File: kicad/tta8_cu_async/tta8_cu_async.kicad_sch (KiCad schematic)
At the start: 23 parts, among them J1 Conn_02x32_Counter_Clockwise, J2 Conn_01x06, J3 Conn_02x02_Odd_Even, U1 74AHCT74, U10 74HCT193, U11 74HCT193, U12 74AHCT00, U13 74AHCT573, U14 74AHCT573, U15 74AHCT573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

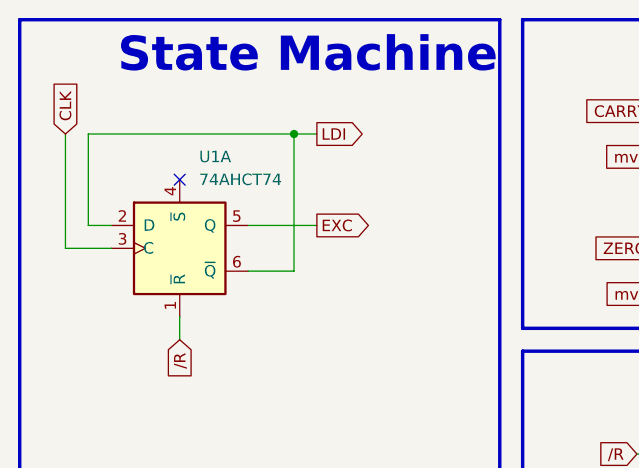
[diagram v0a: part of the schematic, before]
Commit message: Fix floating /S in State Machine
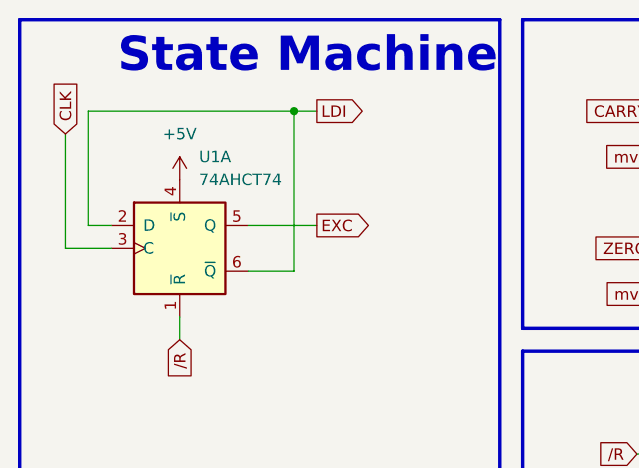
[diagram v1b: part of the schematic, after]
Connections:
- net +5V: now also U1.4 (~{S})
- no-connect marks 26 -> 25
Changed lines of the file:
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@@
 	)
 	(junction
-		(at 369.57 104.14)
+		(at 44.45 24.13)
 		(diameter 0)
 		(color 0 0 0 0)
 	)
 	(junction
-		(at 44.45 26.67)
+		(at 369.57 104.14)
 		(diameter 0)
 		(color 0 0 0 0)
@@
 	)
 	(no_connect
-		(at 31.75 31.75)
-	)
-	(no_connect
 		(at 73.66 138.43)
 	)
@@
 	(wire
 		(pts
-			(xy 44.45 26.67) (xy 46.99 26.67)
+			(xy 44.45 24.13) (xy 46.99 24.13)
 		)
 		(stroke
@@
 	(wire
 		(pts
-			(xy 44.45 26.67) (xy 21.59 26.67)
+			(xy 44.45 24.13) (xy 21.59 24.13)
 		)
 		(stroke
@@
 	(wire
 		(pts
-			(xy 44.45 26.67) (xy 44.45 41.91)
-		)
-		(stroke
-			(width 0)
-			(type default)
-		)
-	)
-	(wire
-		(pts
 			(xy 250.19 43.18) (xy 254 43.18)
 		)
@@
 	(wire
 		(pts
-			(xy 21.59 26.67) (xy 21.59 36.83)
+			(xy 21.59 24.13) (xy 21.59 36.83)
 		)
 		(stroke
@@
 	(wire
 		(pts
+			(xy 44.45 24.13) (xy 44.45 41.91)
+		)
+		(stroke
+			(width 0)
+			(type default)
+		)
+	)
+	(wire
+		(pts
 			(xy 125.73 133.35) (xy 125.73 135.89)
 		)
@@
 	(global_label "LDI"
 		(shape output)
-		(at 46.99 26.67 0)
+		(at 46.99 24.13 0)
 		(fields_autoplaced yes)
 		(effects
@@
 		)
 		(property "Intersheetrefs" "${INTERSHEET_REFS}"
-			(at 52.8781 26.67 0)
+			(at 52.8781 24.13 0)
 			(effects
 				(font
@@
 				)
 			)
+		)
+	)
+	(symbol
+		(lib_id "power:+5V")
+		(at 31.75 31.75 0)
+		(unit 1)
+		(exclude_from_sim no)
+		(in_bom yes)
+		(on_board yes)
+		(dnp no)
+		(fields_autoplaced yes)
+		(property "Reference" "#PWR03"
+			(at 31.75 35.56 0)
+			(effects
+				(font
+					(size 1.27 1.27)
+				)
+				(hide yes)
+			)
+		)
+		(property "Value" "+5V"
+			(at 31.75 26.67 0)
+			(effects
+				(font
+					(size 1.27 1.27)
+				)
+			)
+		)
+		(property "Footprint" ""
+			(at 31.75 31.75 0)
+			(effects
+				(font
+					(size 1.27 1.27)
+				)
+				(hide yes)
+			)
+		)
+		(property "Datasheet" ""
+			(at 31.75 31.75 0)
+			(effects
+				(font
+					(size 1.27 1.27)
+				)
+				(hide yes)
+			)
+		)
+		(property "Description" "Power symbol creates a global label with name \"+5V\""
+			(at 31.75 31.75 0)
+			(effects
+				(font
+					(size 1.27 1.27)
+				)
+				(hide yes)
+			)
+		)
+		(pin "1"
+		)
+		(instances
+			(project "tta8_cu_async"
+				(path "/ee320d24-5d9c-4c33-80b6-742ba44744c6"
+					(reference "#PWR03")
+					(unit 1)
+				)
+			)

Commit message: cu change to sockets
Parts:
- U1, U12, U2, U3: footprint Package_DIP:DIP-14_W7.62mm -> Package_DIP:DIP-14_W7.62mm_Socket
- U10, U11, U5, U6, U7, U8, U9: footprint Package_DIP:DIP-16_W7.62mm -> Package_DIP:DIP-16_W7.62mm_Socket
- U13, U14, U15, U16, U4: footprint Package_DIP:DIP-20_W7.62mm -> Package_DIP:DIP-20_W7.62mm_Socket
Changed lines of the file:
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@@
 			)
 		)
-		(property "Footprint" "Package_DIP:DIP-20_W7.62mm"
+		(property "Footprint" "Package_DIP:DIP-20_W7.62mm_Socket"
 			(at 237.49 53.34 0)
 			(effects
@@
 			)
 		)
-		(property "Footprint" "Package_DIP:DIP-14_W7.62mm"
+		(property "Footprint" "Package_DIP:DIP-14_W7.62mm_Socket"
 			(at 344.17 212.09 0)
 			(effects
@@
 			)
 		)
-		(property "Footprint" "Package_DIP:DIP-14_W7.62mm"
+		(property "Footprint" "Package_DIP:DIP-14_W7.62mm_Socket"
 			(at 322.58 212.09 0)
 			(effects
@@
 			)
 		)
-		(property "Footprint" "Package_DIP:DIP-20_W7.62mm"
+		(property "Footprint" "Package_DIP:DIP-20_W7.62mm_Socket"
 			(at 36.83 105.41 0)
 			(effects
@@
 			)
 		)
-		(property "Footprint" "Package_DIP:DIP-14_W7.62mm"
+		(property "Footprint" "Package_DIP:DIP-14_W7.62mm_Socket"
 			(at 115.57 34.29 0)
 			(effects
@@
 			)
 		)
-		(property "Footprint" "Package_DIP:DIP-20_W7.62mm"
+		(property "Footprint" "Package_DIP:DIP-20_W7.62mm_Socket"
 			(at 384.81 106.68 0)
 			(effects
@@
 			)
 		)
-		(property "Footprint" "Package_DIP:DIP-16_W7.62mm"
+		(property "Footprint" "Package_DIP:DIP-16_W7.62mm_Socket"
 			(at 63.5 130.81 0)
 			(effects
@@
 			)
 		)
-		(property "Footprint" "Package_DIP:DIP-14_W7.62mm"
+		(property "Footprint" "Package_DIP:DIP-14_W7.62mm_Socket"
 			(at 95.25 41.91 0)
 			(effects
@@
 			)
 		)
-		(property "Footprint" "Package_DIP:DIP-16_W7.62mm"
+		(property "Footprint" "Package_DIP:DIP-16_W7.62mm_Socket"
 			(at 280.67 106.68 0)
 			(effects
@@
 			)
 		)
-		(property "Footprint" "Package_DIP:DIP-16_W7.62mm"
+		(property "Footprint" "Package_DIP:DIP-16_W7.62mm_Socket"
 			(at 137.16 130.81 0)
 			(effects
@@
 			)
 		)
-		(property "Footprint" "Package_DIP:DIP-14_W7.62mm"
+		(property "Footprint" "Package_DIP:DIP-14_W7.62mm_Socket"
 			(at 375.92 140.97 0)
 			(effects
@@
 			)
 		)
-		(property "Footprint" "Package_DIP:DIP-14_W7.62mm"
+		(property "Footprint" "Package_DIP:DIP-14_W7.62mm_Socket"
 			(at 391.16 176.53 0)
 			(effects
@@
 			)
 		)
-		(property "Footprint" "Package_DIP:DIP-20_W7.62mm"
+		(property "Footprint" "Package_DIP:DIP-20_W7.62mm_Socket"
 			(at 318.77 53.34 0)
 			(effects
@@
 			)
 		)
-		(property "Footprint" "Package_DIP:DIP-14_W7.62mm"
+		(property "Footprint" "Package_DIP:DIP-14_W7.62mm_Socket"
 			(at 133.35 36.83 0)
 			(effects
@@
 			)
 		)
-		(property "Footprint" "Package_DIP:DIP-14_W7.62mm"
+		(property "Footprint" "Package_DIP:DIP-14_W7.62mm_Socket"
 			(at 345.44 176.53 0)
 			(effects
@@
 			)
 		)
-		(property "Footprint" "Package_DIP:DIP-14_W7.62mm"
+		(property "Footprint" "Package_DIP:DIP-14_W7.62mm_Socket"
 			(at 203.2 66.04 0)
 			(effects
@@
 			)
 		)
-		(property "Footprint" "Package_DIP:DIP-16_W7.62mm"
+		(property "Footprint" "Package_DIP:DIP-16_W7.62mm_Socket"
 			(at 199.39 106.68 0)
 			(effects
@@
 			)
 		)
-		(property "Footprint" "Package_DIP:DIP-14_W7.62mm"
+		(property "Footprint" "Package_DIP:DIP-14_W7.62mm_Socket"
 			(at 365.76 212.09 0)
 			(effects
@@
 			)
 		)
-		(property "Footprint" "Package_DIP:DIP-16_W7.62mm"
+		(property "Footprint" "Package_DIP:DIP-16_W7.62mm_Socket"
 			(at 321.31 106.68 0)
 			(effects
@@
 			)
 		)
-		(property "Footprint" "Package_DIP:DIP-16_W7.62mm"
+		(property "Footprint" "Package_DIP:DIP-16_W7.62mm_Socket"
 			(at 100.33 130.81 0)
 			(effects
@@
 			)
 		)
-		(property "Footprint" "Package_DIP:DIP-14_W7.62mm"
+		(property "Footprint" "Package_DIP:DIP-14_W7.62mm_Socket"
 			(at 151.13 39.37 0)
 			(effects
@@
 			)
 		)
-		(property "Footprint" "Package_DIP:DIP-14_W7.62mm"
+		(property "Footprint" "Package_DIP:DIP-14_W7.62mm_Socket"
 			(at 95.25 64.77 0)
 			(effects
@@
 			)
 		)
-		(property "Footprint" "Package_DIP:DIP-16_W7.62mm"
+		(property "Footprint" "Package_DIP:DIP-16_W7.62mm_Socket"
 			(at 240.03 106.68 0)
 			(effects
@@
 			)
 		)
-		(property "Footprint" "Package_DIP:DIP-14_W7.62mm"
+		(property "Footprint" "Package_DIP:DIP-14_W7.62mm_Socket"
 			(at 368.3 176.53 0)
 			(effects
@@
 			)
 		)
-		(property "Footprint" "Package_DIP:DIP-14_W7.62mm"
+		(property "Footprint" "Package_DIP:DIP-14_W7.62mm_Socket"
 			(at 322.58 176.53 0)
 			(effects
@@
 			)
 		)
-		(property "Footprint" "Package_DIP:DIP-14_W7.62mm"
+		(property "Footprint" "Package_DIP:DIP-14_W7.62mm_Socket"
 			(at 387.35 212.09 0)
 			(effects
@@
 			)
 		)
-		(property "Footprint" "Package_DIP:DIP-20_W7.62mm"
+		(property "Footprint" "Package_DIP:DIP-20_W7.62mm_Socket"
 			(at 384.81 50.8 0)
 			(effects
@@
 			)
 		)
-		(property "Footprint" "Package_DIP:DIP-14_W7.62mm"
+		(property "Footprint" "Package_DIP:DIP-14_W7.62mm_Socket"
 			(at 330.2 140.97 0)
 			(effects
@@
 			)
 		)
-		(property "Footprint" "Package_DIP:DIP-14_W7.62mm"
+		(property "Footprint" "Package_DIP:DIP-14_W7.62mm_Socket"
 			(at 95.25 26.67 0)
 			(effects
@@
 			)
 		)
-		(property "Footprint" "Package_DIP:DIP-14_W7.62mm"
+		(property "Footprint" "Package_DIP:DIP-14_W7.62mm_Socket"
 			(at 31.75 39.37 0)
 			(effects
